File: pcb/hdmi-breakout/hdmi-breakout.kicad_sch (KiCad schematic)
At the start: 5 parts, among them J1 Conn_01x02, J2 HDMI_A_1.4, J3 HDMI_A_1.4, J4 Conn_01x02, U1 XIAO-RP2350-DIP

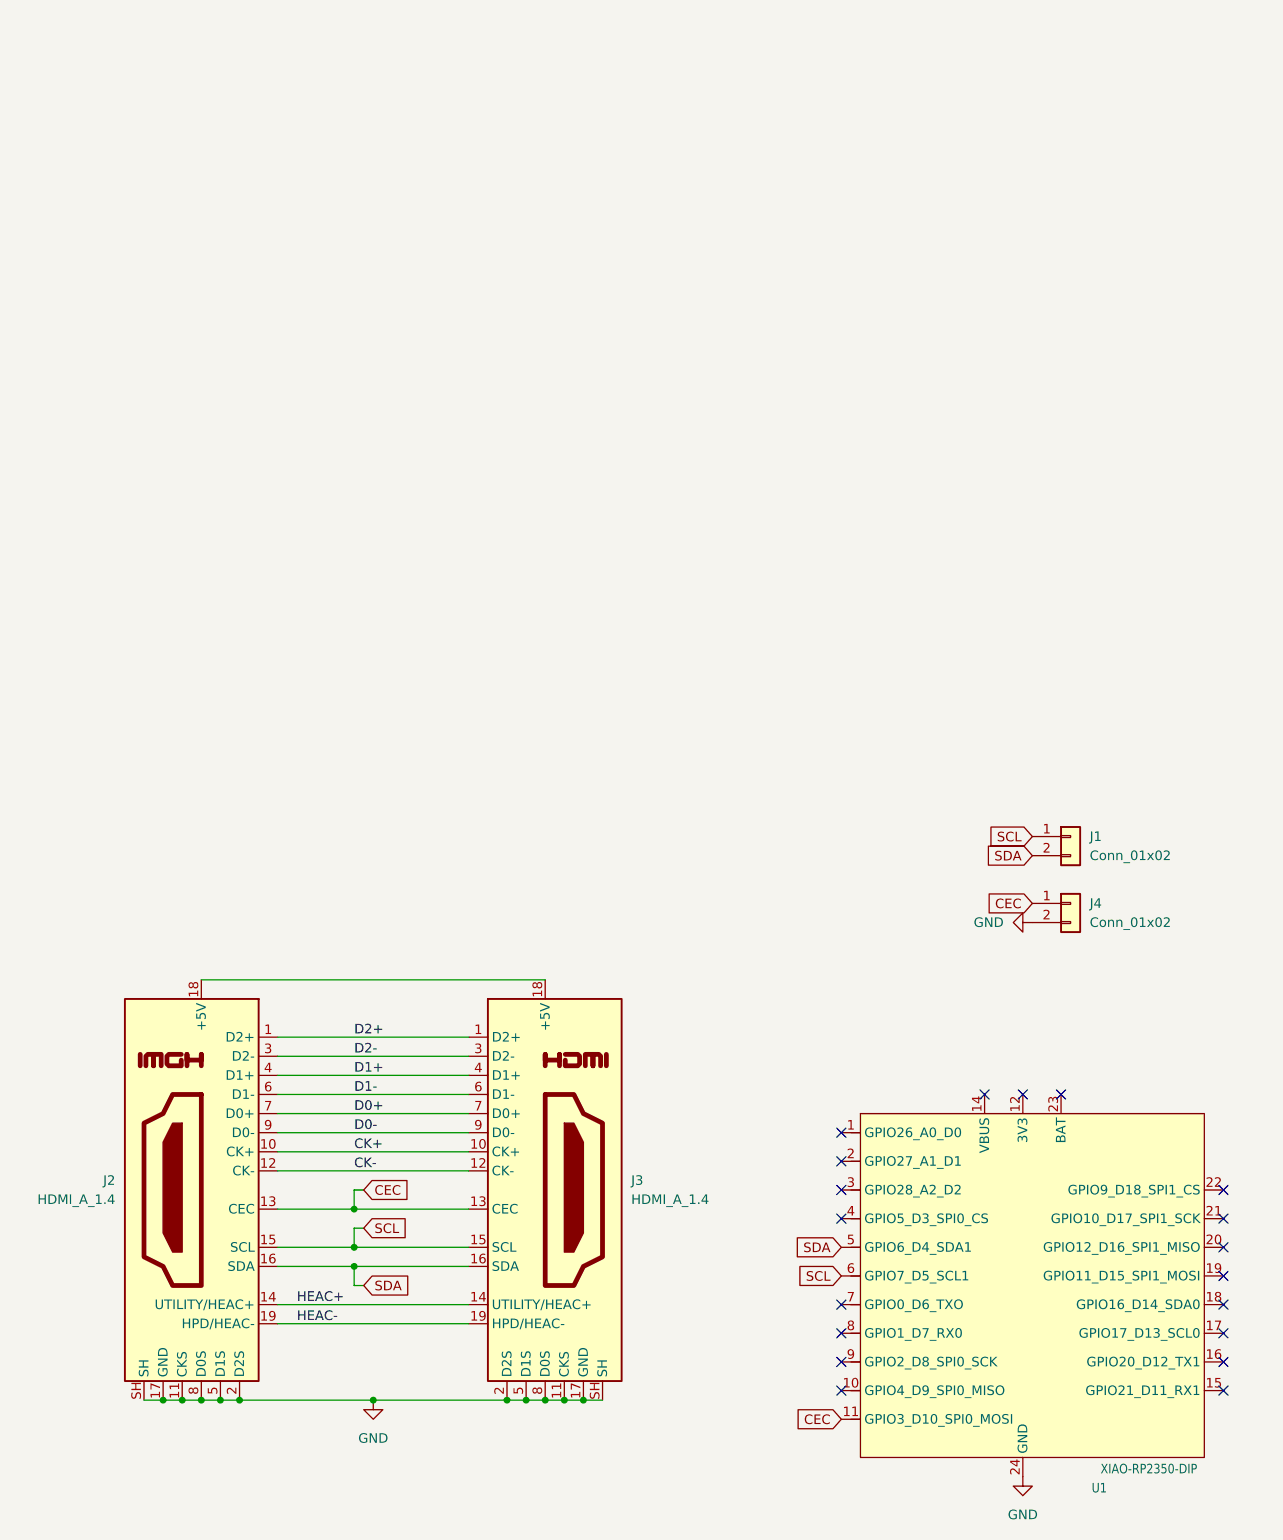
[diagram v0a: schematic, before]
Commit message: fix some fatal bugs, migrate to rp2040-zero
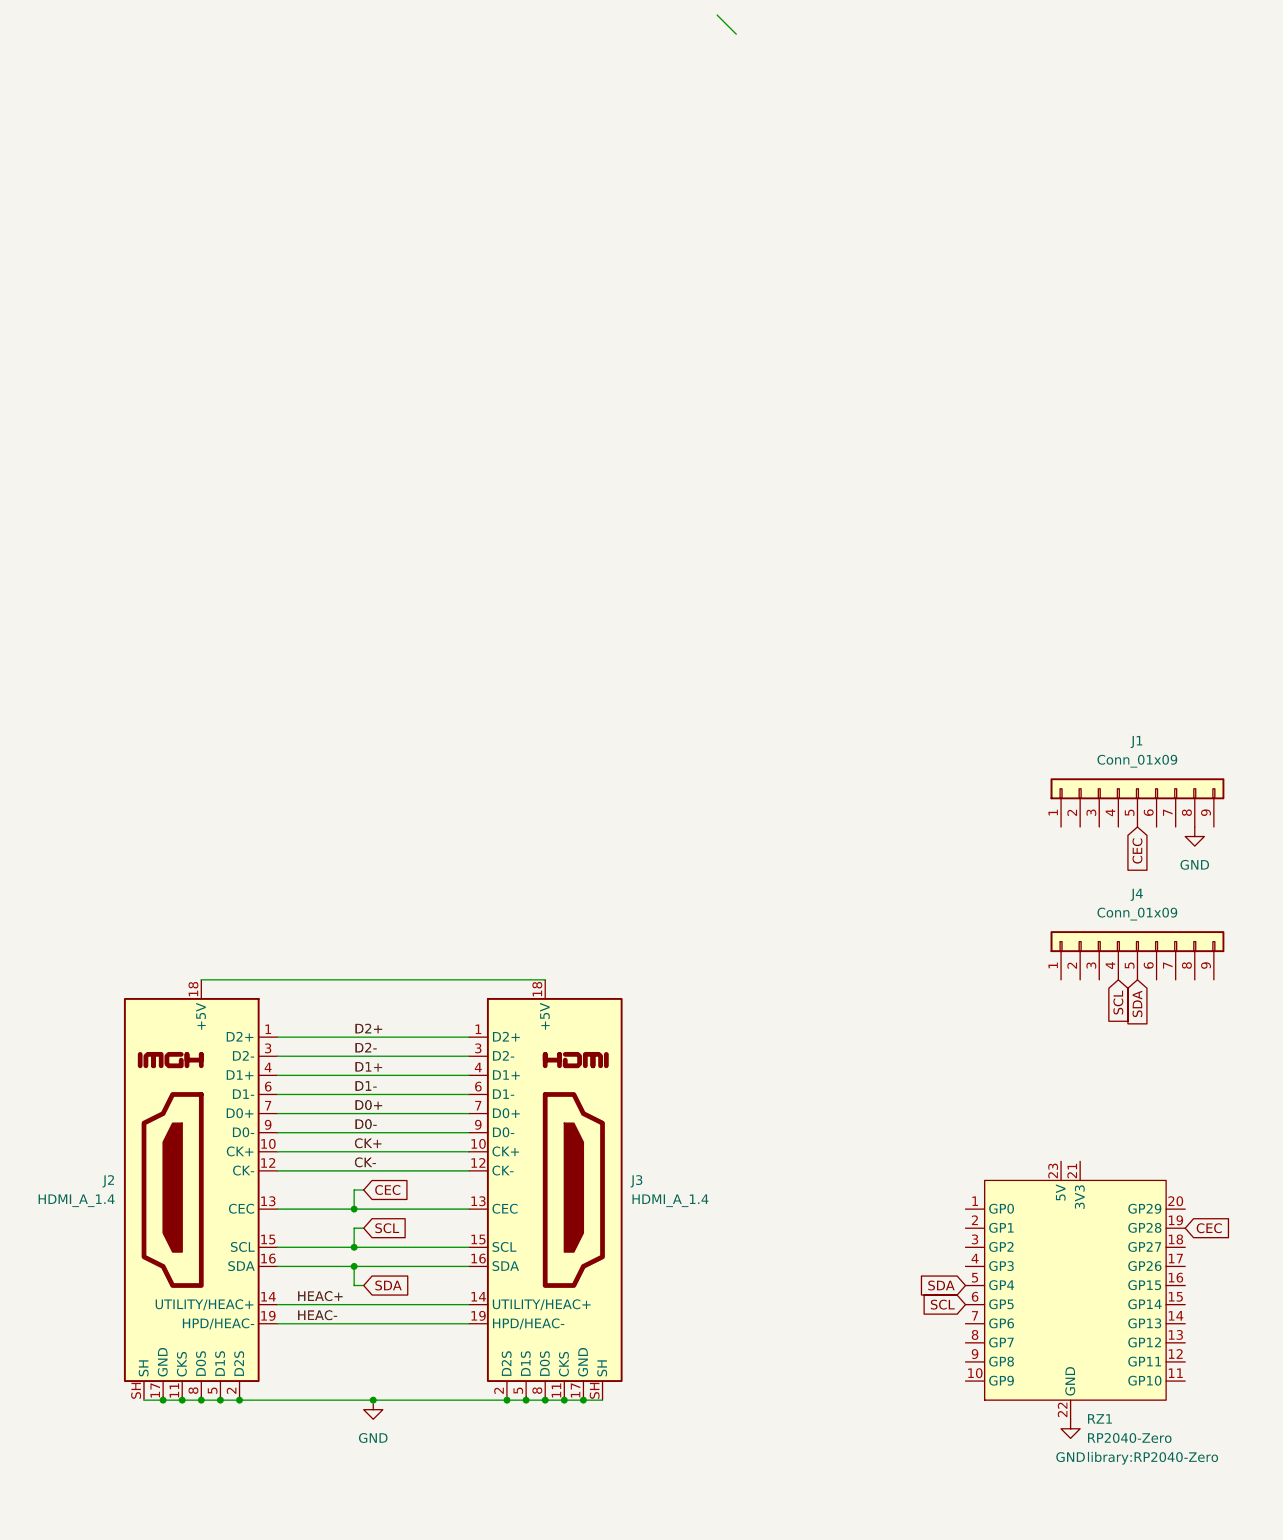
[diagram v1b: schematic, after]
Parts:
- removed J1, J4: Conn_01x02, Connector_PinHeader_2.54mm:PinHeader_1x02_P2.54mm_Vertical, symbol Connector_Generic:Conn_01x02
- removed U1: XIAO-RP2350-DIP, library:XIAO-RP2350-DIP, symbol Seeed_Studio_XIAO_Series:XIAO-RP2350-DIP
- added J1, J4: Conn_01x09, Connector_PinHeader_2.54mm:PinHeader_1x09_P2.54mm_Vertical, symbol Connector_Generic:Conn_01x09
- added RZ1: RP2040-Zero, library:RP2040-Zero, symbol rp2040-zero:RP2040-Zero
- J2: footprint library:HDMI_A_Molex_208658-1001_Horizontal_Mirror -> Connector_Video:HDMI_A_Molex_208658-1001_Horizontal
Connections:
- net CEC: now also J1.5 (Pin_5), RZ1.19 (GP28)
- net GND: now also J1.8 (Pin_8), RZ1.22 (GND)
- net SCL: now also J4.4 (Pin_4), RZ1.6 (GP5)
- net SDA: now also J4.5 (Pin_5), RZ1.5 (GP4)
- no-connect marks 19 -> 0

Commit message: update docs
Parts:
- removed RZ1: RP2040-Zero, library:RP2040-Zero, symbol rp2040-zero:RP2040-Zero
